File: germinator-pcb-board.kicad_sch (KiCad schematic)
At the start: 0 parts

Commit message: Schematics step 2: symbols added
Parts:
- added J1, J2: Conn_01x15_Socket, symbol Connector:Conn_01x15_Socket
- added J3: Screw_Terminal_01x04, symbol Connector:Screw_Terminal_01x04
- added J4, J5, J6, J7: Screw_Terminal_01x03, symbol Connector:Screw_Terminal_01x03
- added R1, R2: R, symbol Device:R
- added U1: ESP32-DEVKIT-V1, germinator-pcb-board-libraries:ESP32_DEVKIT_V1, symbol ESP32-DEVKIT-V1:ESP32-DEVKIT-V1
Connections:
- new net: U1.2 (GND), U1.29 (GND)

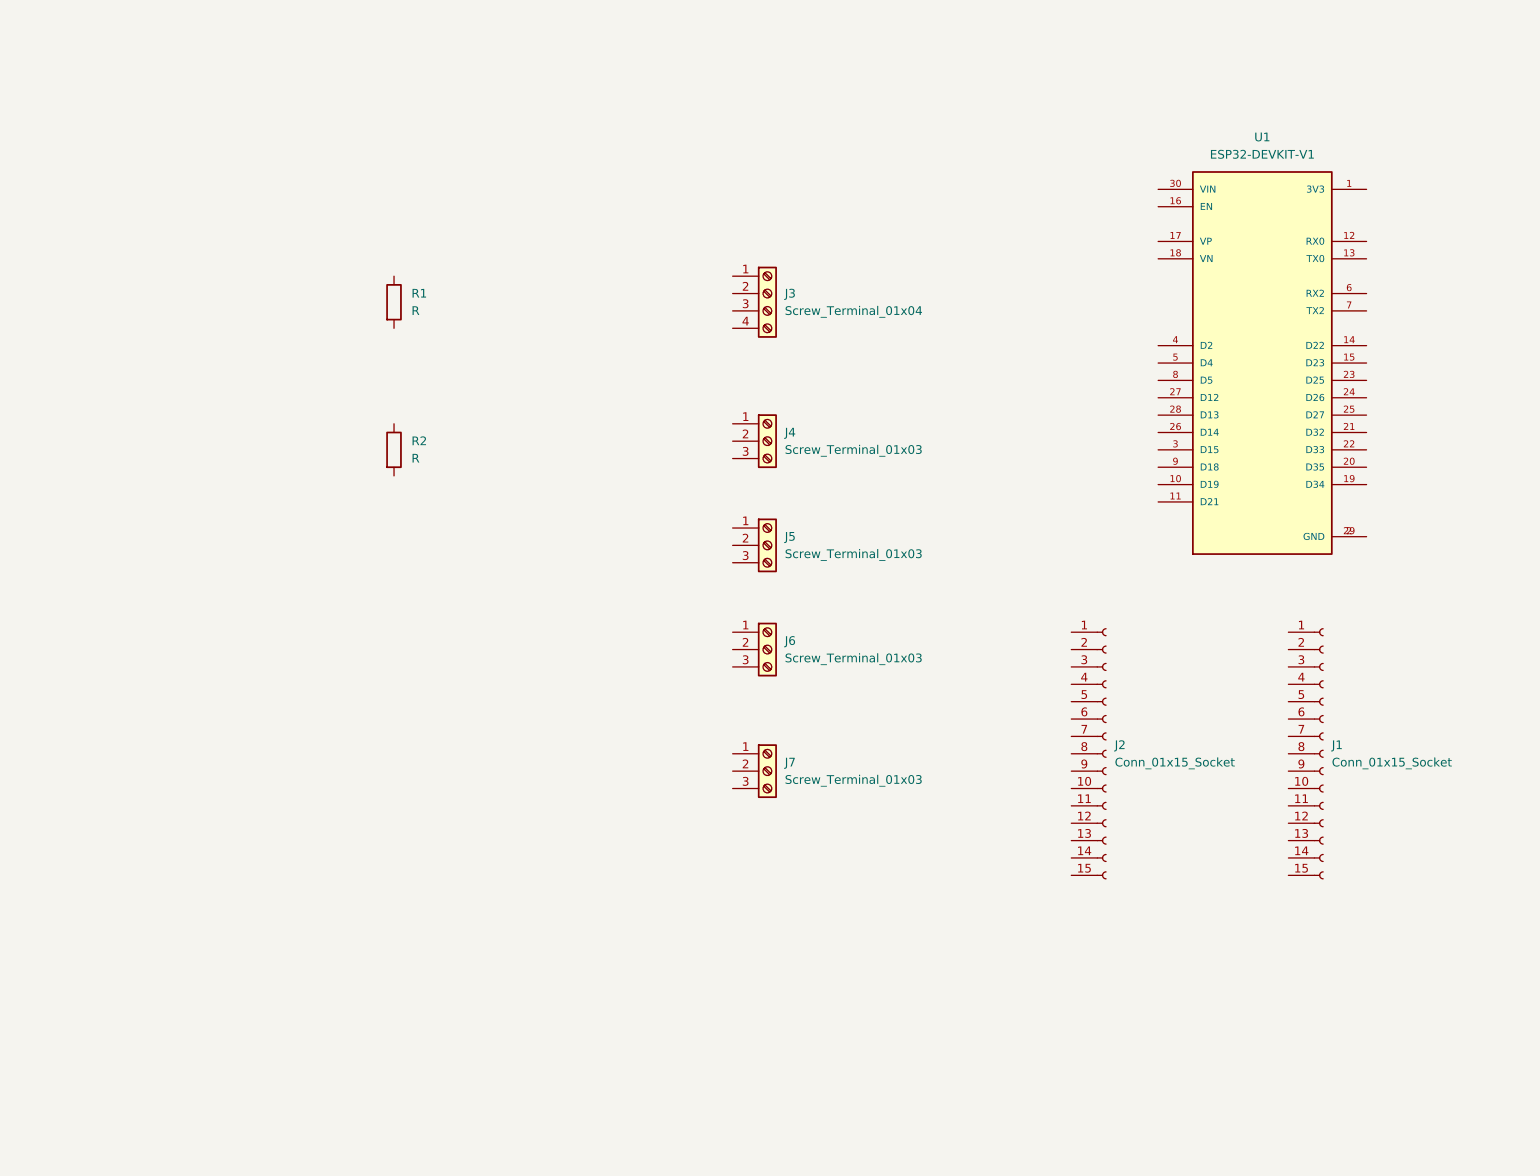
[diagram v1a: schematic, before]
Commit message: Schematics step 3: Arrange and Annotate
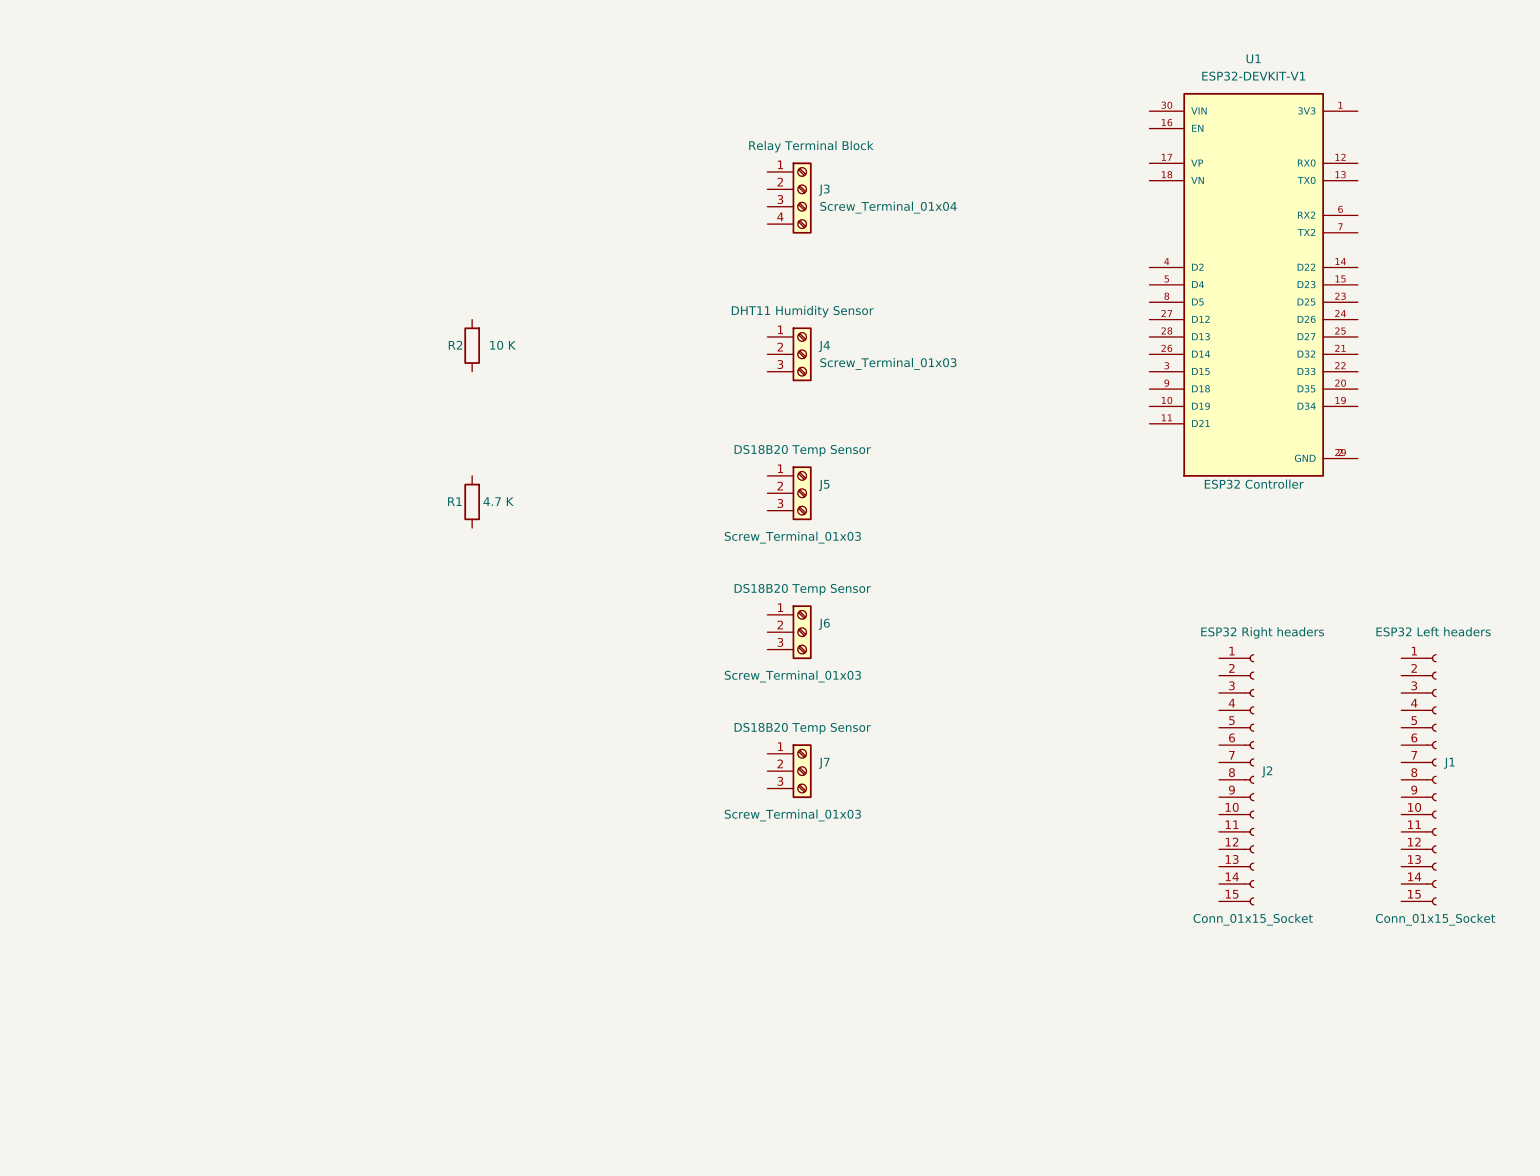
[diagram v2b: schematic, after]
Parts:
- J1: Purpose (none) -> ESP32 Left headers
- J2: Purpose (none) -> ESP32 Right headers
- J3: footprint (none) -> TerminalBlock:TerminalBlock_MaiXu_MX126-5.0-04P_1x04_P5.00mm; Purpose (none) -> Relay Terminal Block
- J4: footprint (none) -> TerminalBlock:TerminalBlock_MaiXu_MX126-5.0-03P_1x03_P5.00mm; Purpose (none) -> DHT11 Humidity Sensor
- J5, J6, J7: footprint (none) -> TerminalBlock:TerminalBlock_MaiXu_MX126-5.0-03P_1x03_P5.00mm; Purpose (none) -> DS18B20 Temp Sensor
- R1: value R -> 4.7 K; footprint (none) -> Resistor_THT:R_Axial_DIN0207_L6.3mm_D2.5mm_P7.62mm_Horizontal; Purpose (none) -> DS18B20 Temp Sensor Pullup
- R2: value R -> 10 K; footprint (none) -> Resistor_THT:R_Axial_DIN0207_L6.3mm_D2.5mm_P7.62mm_Horizontal; Purpose (none) -> DHT11 Pullup
- U1: Purpose (none) -> ESP32 Controller
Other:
- moved on the sheet: J1, J2, J3, J4, J5, J6, J7, R1, R2, U1

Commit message: Schematics step 4: Wiring
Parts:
- U1: footprint germinator-pcb-board-libraries:ESP32_DEVKIT_V1 -> ESP32-DEVKIT-V1:MODULE_ESP32_DEVKIT_V1; Availability (none) -> Not in stock; Check_prices (none) -> https://www.snapeda.com/parts/ESP32-DEVKIT-V1/Do+it/view-pa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; Description_1 (none) -> Dual core, Wi-Fi: 2.4 GHz up to 150 Mbits/s,BLE (Bluetooth 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; MAXIMUM_PACKAGE_HEIGHT (none) -> 6.8 mm; MF (none) -> Do it; MP (none) -> ESP32-DEVKIT-V1; PARTREV (none) -> N/A; Package (none) -> None; Price (none) -> None; STANDARD (none) -> Manufacturer Recommendations; SnapEDA_Link (none) -> https://www.snapeda.com/parts/ESP32-DEVKIT-V1/Do+it/view-pa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
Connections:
- net Vcc: now reaches J6.1 (Pin_1)
- net Vcc: now also J3.1 (Pin_1), J4.1 (Pin_1), J5.1 (Pin_1), J7.1 (Pin_1), R1.2, R2.2, U1.1 (3V3)
- net D15: now reaches J6.2 (Pin_2)
- net D15: now also J2.13 (Pin_13), J5.2 (Pin_2), J7.2 (Pin_2), R1.1, U1.3 (D15)
- net GND: now reaches J6.3 (Pin_3)
- net GND: now also J1.14 (Pin_14), J2.14 (Pin_14), J3.4 (Pin_4), J4.3 (Pin_3), J5.3 (Pin_3), J7.3 (Pin_3), U1.2 (GND), U1.29 (GND)
- net D25: now reaches J3.2 (Pin_2)
- net D25: now also J1.8 (Pin_8), U1.23 (D25)
- net D26: now reaches J3.3 (Pin_3)
- net D26: now also J1.9 (Pin_9), U1.24 (D26)
- net EN: now reaches J1.1 (Pin_1)
- net EN: now also U1.16 (EN)
- net D27: now reaches J1.10 (Pin_10)
- net D27: now also U1.25 (D27)
- net D14: now reaches J1.11 (Pin_11)
- net D14: now also U1.26 (D14)
- net D12: now reaches J1.12 (Pin_12)
- net D12: now also U1.27 (D12)
- net D13: now reaches J1.13 (Pin_13)
- net D13: now also U1.28 (D13)
- net VIN: now reaches J1.15 (Pin_15)
- net VIN: now also U1.30 (VIN)
- net VP: now reaches J1.2 (Pin_2)
- net VP: now also U1.17 (VP)
- net VN: now reaches J1.3 (Pin_3)
- net VN: now also U1.18 (VN)
- net D34: now reaches J1.4 (Pin_4)
- net D35: now reaches J1.5 (Pin_5)
- net D35: now also U1.20 (D35)
- net D32: now reaches J1.6 (Pin_6)
- net D32: now also U1.21 (D32)
- net D33: now reaches J1.7 (Pin_7)
- net D33: now also U1.22 (D33)
- net D23: now reaches J2.1 (Pin_1)
- net D23: now also U1.15 (D23)
- net RX2: now reaches J2.10 (Pin_10)
- net RX2: now also U1.6 (RX2)
- net D4: now reaches J2.11 (Pin_11)
- net D4: now also J4.2 (Pin_2), R2.1, U1.5 (D4)
- net D2: now reaches J2.12 (Pin_12)
- net D2: now also U1.4 (D2)
- net VCC: now reaches J2.15 (Pin_15)
- net D22: now reaches J2.2 (Pin_2)
- net D22: now also U1.14 (D22)
- net TX0: now reaches J2.3 (Pin_3)
- net TX0: now also U1.13 (TX0)
- net RX0: now reaches J2.4 (Pin_4)
- net RX0: now also U1.12 (RX0)
- net D21: now reaches J2.5 (Pin_5)
- net D21: now also U1.11 (D21)
- net D19: now reaches J2.6 (Pin_6)
- net D19: now also U1.10 (D19)
- net D18: now reaches J2.7 (Pin_7)
- net D18: now also U1.9 (D18)
- net D5: now reaches J2.8 (Pin_8)
- net D5: now also U1.8 (D5)
- net TX2: now reaches J2.9 (Pin_9)
- net TX2: now also U1.7 (TX2)
- net D43: now reaches U1.19 (D34)
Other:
- moved on the sheet: J1, J2, J3, J4, J5, J6, J7, R1, R2

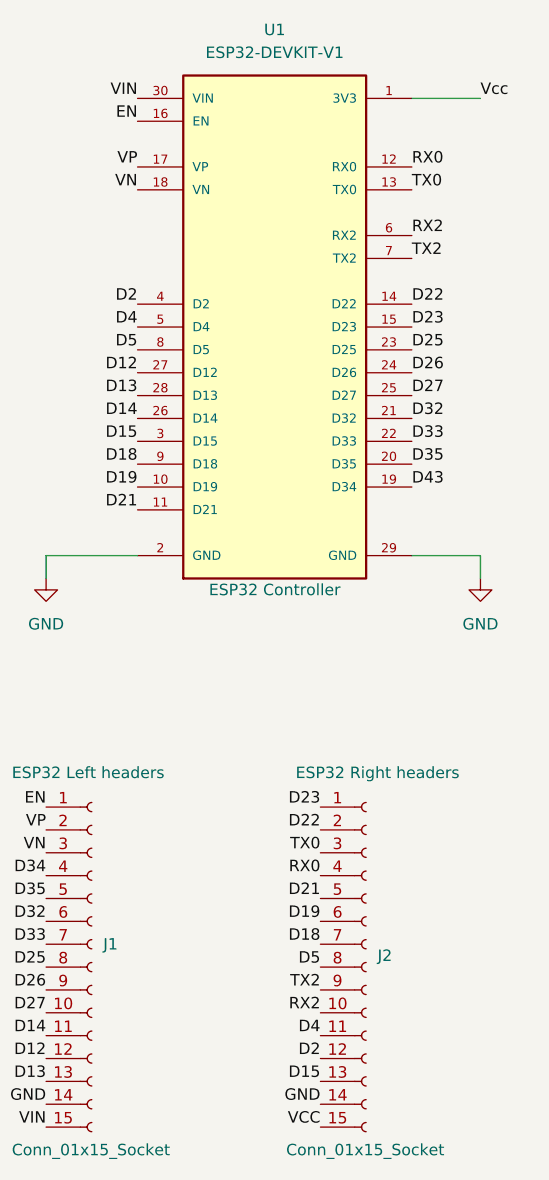
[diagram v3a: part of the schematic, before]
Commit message: Schematics step 5 & 6: Nets and Electric rules checking
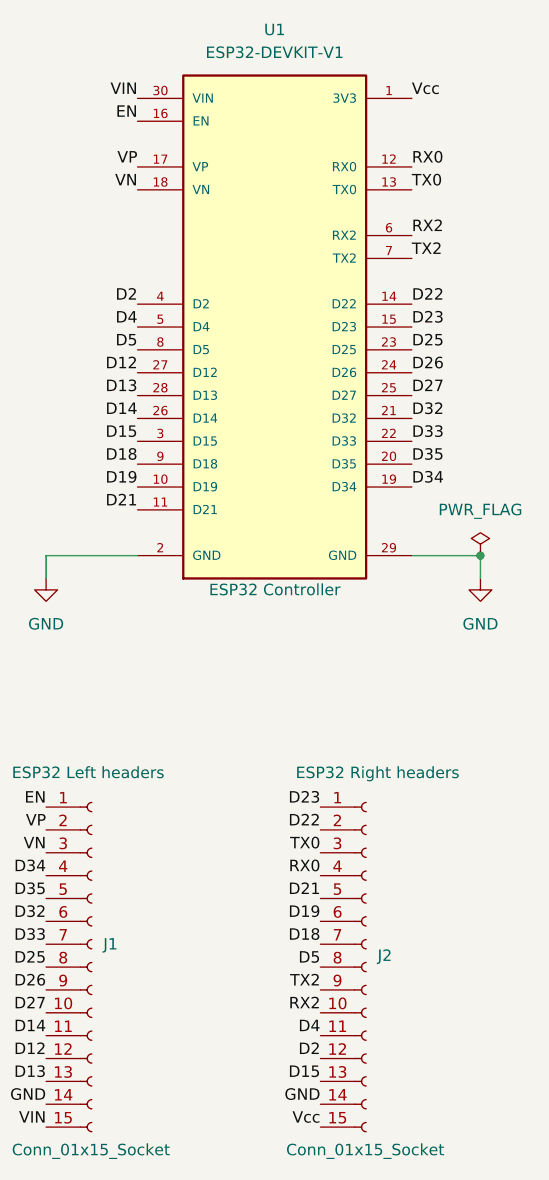
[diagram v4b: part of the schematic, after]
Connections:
- net D43 is gone; now on net D34: U1.19 (D34)
- net VCC is gone; now on net Vcc: J2.15 (Pin_15)
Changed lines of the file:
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@@
+	)
+	(junction
+		(at 254 88.9)
+		(diameter 0)
+		(color 0 0 0 0)
 	)
 	(junction
@@
 	(wire
 		(pts
-			(xy 246.38 38.1) (xy 254 38.1)
-		)
-		(stroke
-			(width 0)
-			(type default)
-		)
-	)
-	(wire
-		(pts
 			(xy 101.6 57.15) (xy 121.92 57.15)
 		)
@@
 		)
 	)
-	(label "D43"
+	(label "D34"
 		(at 246.38 81.28 0)
 		(effects
@@
 	)
 	(label "Vcc"
-		(at 254 38.1 0)
+		(at 246.38 38.1 0)
 		(effects
 			(font
@@
 		)
 	)
-	(label "VCC"
+	(label "Vcc"
 		(at 236.22 152.4 180)
 		(effects
@@
 					(unit 1)
 				)
+			)
+		)
+	)
+	(symbol
+		(lib_id "power:PWR_FLAG")
+		(at 254 88.9 0)
+		(unit 1)
+		(exclude_from_sim no)
+		(in_bom yes)
+		(on_board yes)
+		(dnp no)
+		(fields_autoplaced yes)
+		(property "Reference" "#FLG02"
+			(at 254 86.995 0)
+			(effects
+				(font
+					(size 1.27 1.27)
+				)
+				(hide yes)
+			)
+		)
+		(property "Value" "PWR_FLAG"
+			(at 254 83.82 0)
+			(effects
+				(font
+					(size 1.27 1.27)
+				)
+			)
+		)
+		(property "Footprint" ""
+			(at 254 88.9 0)
+			(effects
+				(font
+					(size 1.27 1.27)
+				)
+				(hide yes)
+			)
+		)
+		(property "Datasheet" "~"
+			(at 254 88.9 0)
+			(effects
+				(font
+					(size 1.27 1.27)
+				)
+				(hide yes)
+			)
+		)
+		(property "Description" "Special symbol for telling ERC where power comes from"
+			(at 254 88.9 0)
+			(effects
+				(font
+					(size 1.27 1.27)
+				)
+				(hide yes)
+			)
+		)
+		(pin "1"
+		)
+		(instances
+			(project ""
+				(path "/bff22e99-e22b-4758-82e3-846916dce764"
+					(reference "#FLG02")
+					(unit 1)
+				)

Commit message: Schematics step 7: Comments
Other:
- note added: "ESP32 DEV KIT V1"
- note added: "Environmental Humidity and Temperature Sensor"
- note added: "Headers to the ESP32 for future use"
- note added: "If using a KY-015 sensor, then there is no need to mount this pullup resistor"
- note added: "Relay Terminal Block"
- note added: "Temperature Sensors"
- moved on the sheet: J1, J2, J3, J4, J5, J6, J7, R1, R2, U1
